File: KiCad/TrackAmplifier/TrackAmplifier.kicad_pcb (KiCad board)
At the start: 2 copper layers, 84 parts, among them J1 DB15_Male_MountingHoles, J2 Conn_01x06, Q1 2N7002, U1 ST485EBDR, U2 ST485EBDR, U3 LM78M05_TO252, U4 LMD18200, U5 ST485EBDR, U6 ST485EBDR, U7 INA326, U8 INA326, U9 PIC16F18854-SO

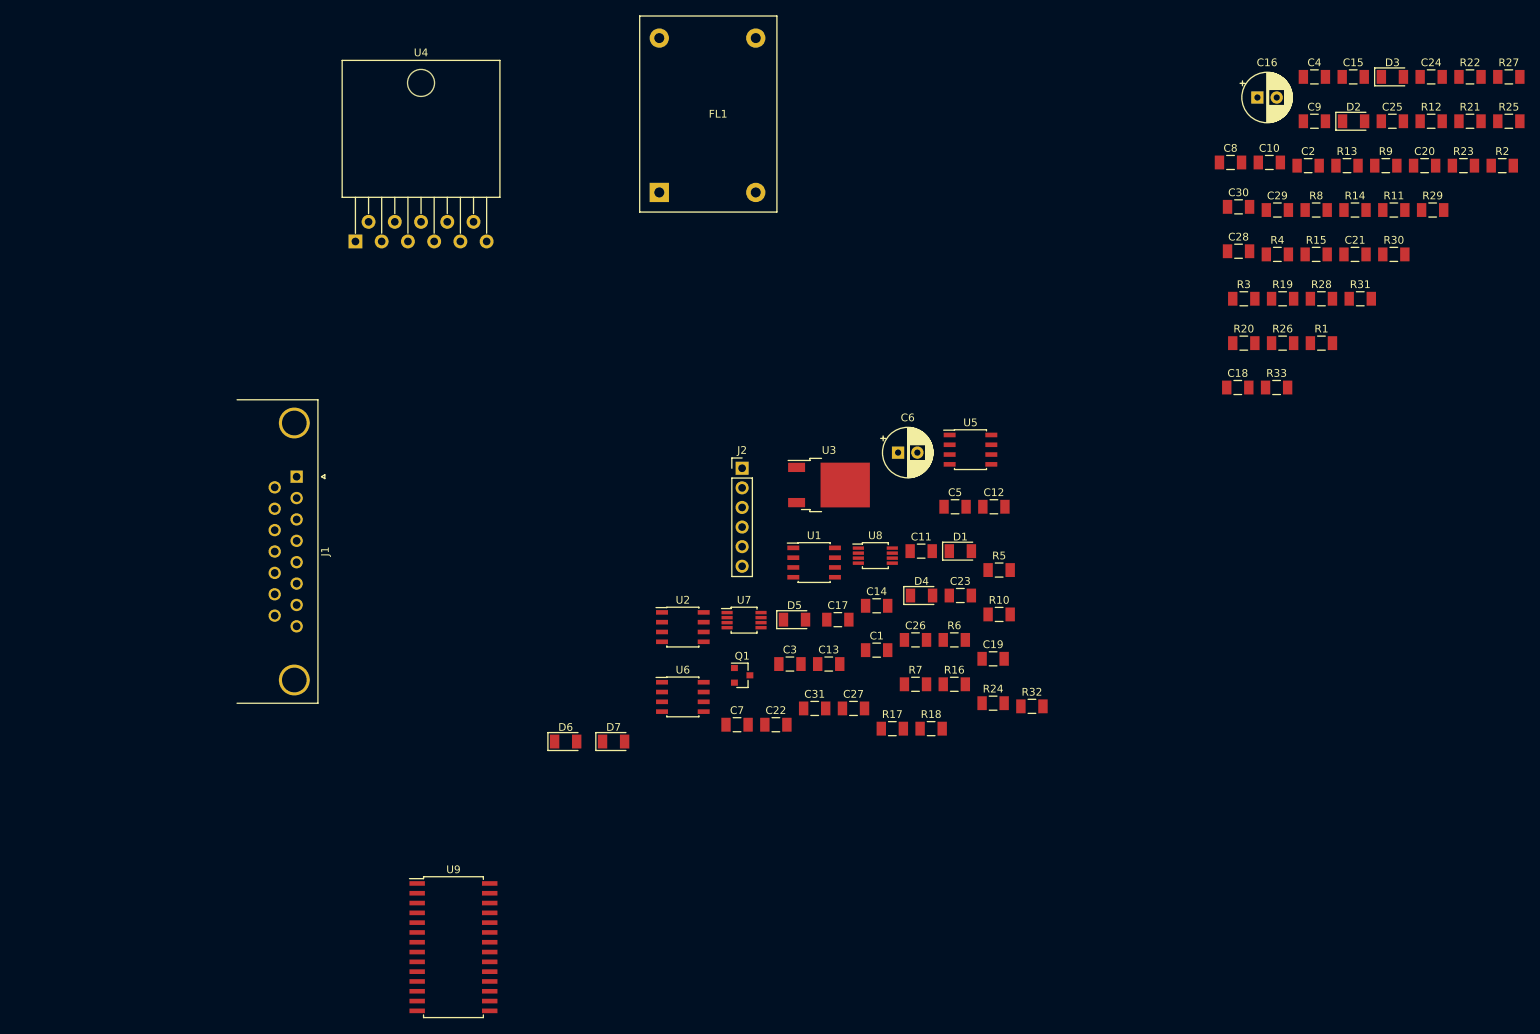
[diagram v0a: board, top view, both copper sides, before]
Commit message: Updated TrackAmplifier.sch and started layout. todo: - verify ina use - verify ref use and connections
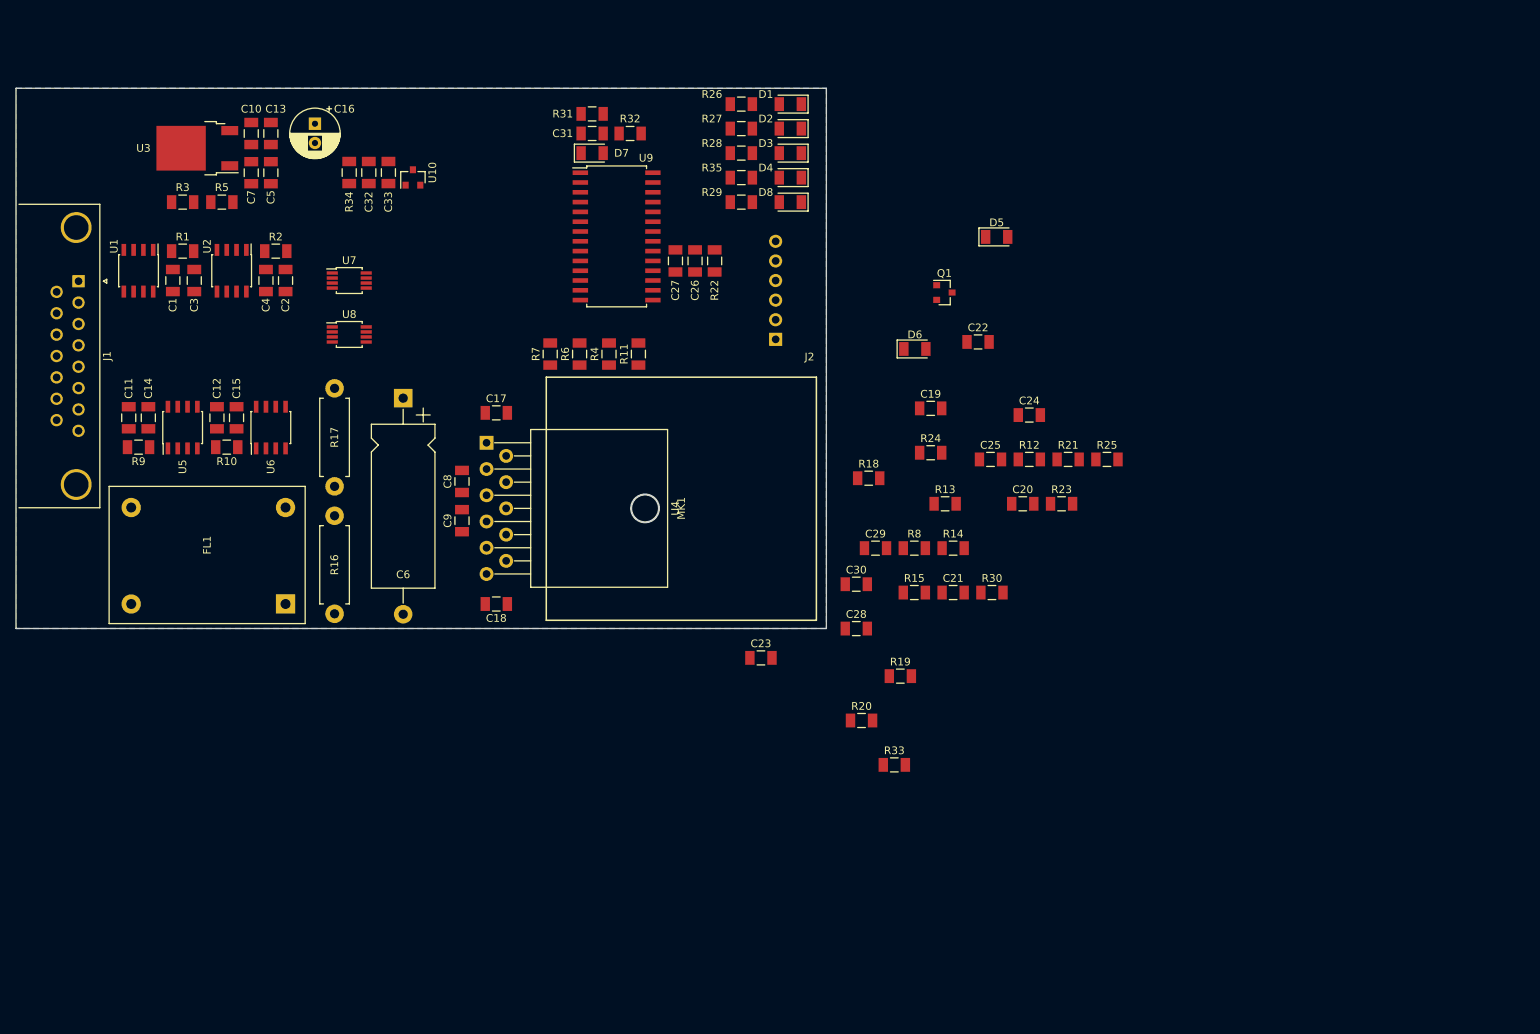
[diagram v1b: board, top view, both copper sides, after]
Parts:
- added C32: 22u, Capacitor_SMD:C_1206_3216Metric, F.Cu at (95.7, 60.9)
- added C33: 100n, Capacitor_SMD:C_1206_3216Metric, F.Cu at (98.3, 60.9)
- added D8: LED, LED_SMD:LED_1206_3216Metric, F.Cu at (150.3, 64.8)
- added MK1: Mounting_Hole, MountingHole:MountingHole_3.7mm, F.Cu at (131.5, 104.4)
- added R34: 10E, Resistor_SMD:R_1206_3216Metric, F.Cu at (93.2, 60.9)
- added R35: 330E, Resistor_SMD:R_1206_3216Metric, F.Cu at (144.0, 61.6)
- added U10: REF3025, Package_TO_SOT_SMD:SOT-23, F.Cu at (101.4, 61.6)
- C6: value 3000u -> 22u; footprint Capacitor_THT:CP_Radial_D6.3mm_P2.50mm -> Capacitor_THT:CP_Axial_L21.0mm_D8.0mm_P28.00mm_Horizontal
- J2: footprint Connector_PinHeader_2.54mm:PinHeader_1x06_P2.54mm_Vertical -> Connector_PinHeader_2.54mm:PinHeader_1x06_P2.54mm_Horizontal; moved to B.Cu
- R16, R17: footprint Resistor_SMD:R_1206_3216Metric -> Resistor_THT:R_Axial_DIN0411_L9.9mm_D3.6mm_P12.70mm_Horizontal
- moved R9 165.7 mm to (65.9, 96.5), turned to 180 degrees
- moved R2 159.3 mm to (83.7, 71.1)
- moved C15 151.3 mm to (78.6, 92.7), turned to 90 degrees
- moved R1 148.0 mm to (71.6, 71.1)
- moved C4 138.4 mm to (82.4, 74.9), turned to 270 degrees
- moved R3 138.1 mm to (71.6, 64.8)
- moved C2 133.3 mm to (84.9, 74.9), turned to 270 degrees
- moved C10 132.0 mm to (80.5, 55.9), turned to 90 degrees
- moved C16 122.2 mm to (88.7, 54.6), turned to 270 degrees
- moved C9 122.0 mm to (107.8, 106.0), turned to 90 degrees
- moved R5 111.4 mm to (76.7, 64.8)
- moved C8 107.8 mm to (107.8, 101.0), turned to 90 degrees
- moved C11 104.1 mm to (64.6, 92.7), turned to 90 degrees
- moved C1 103.0 mm to (70.3, 74.9), turned to 270 degrees
- moved R10 102.4 mm to (77.3, 96.5), turned to 180 degrees
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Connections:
- C21 pad 2: Net-(C21-Pad2) -> REF
- C25 pad 2: Net-(C25-Pad2) -> REF
- C30 pad 1: Net-(C30-Pad1) -> GND
- C6 pad 1: +15V -> VBUS
- C8 pad 2: +15V -> VBUS
- C9 pad 2: +15V -> VBUS
- J1 pad 10: Reset_B -> Reset_A
- J1 pad 11: Sync_B -> Sync_A
- J1 pad 12: RX_B -> RX_A
- J1 pad 3: Reset_A -> Reset_B
- J1 pad 4: Sync_A -> Sync_B
- J1 pad 5: RX_A -> RX_B
- R15 pad 1: Net-(C21-Pad2) -> REF
- R21 pad 1: Net-(C25-Pad2) -> REF
- R29 pad 1: TX_ENA -> Net-(R29-Pad1)
- R29 pad 2: Net-(D4-Pad2) -> Net-(D8-Pad2)
- U4 pad 6: +15V -> VBUS
- U7 pad 5: Net-(C21-Pad2) -> REF
- U8 pad 5: Net-(C25-Pad2) -> REF
- U9 pad 11: BRK -> SYNC
- U9 pad 12: DIR -> TX
- U9 pad 13: PWM -> TX_ENA
- U9 pad 14: SYNC -> RX
- U9 pad 15: THFLG -> DIR
- U9 pad 16: TX_ENA -> BRK
- U9 pad 17: TX -> PWM
- U9 pad 18: RX -> THFLG
- U9 pad 2: ID -> REF
- U9 pad 21: Net-(R28-Pad1) -> CSEN_FLT
- U9 pad 22: Net-(R27-Pad1) -> Net-(R29-Pad1)
- U9 pad 23: Net-(R26-Pad1) -> Net-(R35-Pad2)
- U9 pad 24: Net-(U9-Pad24) -> Net-(R28-Pad1)
- U9 pad 25: Net-(U9-Pad25) -> Net-(R27-Pad1)
- U9 pad 26: Net-(U9-Pad26) -> Net-(R26-Pad1)
- U9 pad 3: BMF -> REF
- U9 pad 4: OCC -> BMF
- U9 pad 5: CSEN_FLT -> OCC
- U9 pad 6: Net-(U9-Pad6) -> ID
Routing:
- added copper zone on B.Cu, net GND
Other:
- board outline added: 105 x 70 mm
- net class Default: trace_width 0.25 -> 0.5; via_dia 0.8 -> 1; via_drill 0.4 -> 0.6
- rule trace_min: 0.2 -> 0.25
- rule via_min_drill: 0.3 -> 0.6
- rule via_min_size: 0.4 -> 1
